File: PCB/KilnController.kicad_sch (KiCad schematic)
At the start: 19 parts, among them J1 12V 3A PS Header, J2 Exhaust Fan Header, J3 Circulation Fan Header, J4 SD Card Module, J5 Exhaust Servo Header, J6 Intake Servo Header, Q1 FQP30N06L, Q2 FQP30N06L, U1 Raspberry Pi Pico 2W

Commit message: Current monitoring WIP
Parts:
- J2, J3, J5, J6: footprint TerminalBlock_MetzConnect:TerminalBlock_MetzConnect_Type101_RT01604HBWC_1x04_P5.08mm_Horizontal -> KilnFootprintLibrary:TerminalBlock_MetzConnect_Type101_RT01604HBWC_1x04_P5.08mm_Horizontal; symbol Connector:Screw_Terminal_01x04 -> KilnSymbols:Screw_Terminal_01x04
- U1: footprint RasPi_Pico:RasPi_Pico_W_SMD -> Module:RaspberryPi_Pico_Common_THT
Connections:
- net SD_MISO: now also U1.6 (GP4); no longer U1.4 (GP2)
- net SD_SCK: now also U1.4 (GP2); no longer U1.6 (GP4)
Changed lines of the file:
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@@
 		)
 	)
-	(label "SD_MISO"
+	(label "SD_SCK"
 		(at 125.73 82.55 180)
 		(effects
@@
 		)
 	)
-	(label "SD_SCK"
+	(label "SD_MISO"
 		(at 125.73 87.63 180)
 		(effects
@@
 	)
 	(symbol
-		(lib_id "Connector:Screw_Terminal_01x04")
+		(lib_id "KilnSymbols:Screw_Terminal_01x04")
 		(at 246.38 134.62 90)
 		(unit 1)
@@
 			)
 		)
-		(property "Footprint" "TerminalBlock_MetzConnect:TerminalBlock_MetzConnect_Type101_RT01604HBWC_1x04_P5.08mm_Horizontal"
+		(property "Footprint" "KilnFootprintLibrary:TerminalBlock_MetzConnect_Type101_RT01604HBWC_1x04_P5.08mm_Horizontal"
 			(at 246.38 134.62 0)
 			(effects
@@
 			)
 		)
-		(property "Footprint" "RasPi_Pico:RasPi_Pico_W_SMD"
+		(property "Footprint" "Module:RaspberryPi_Pico_Common_THT"
 			(at 140.97 99.06 0)
 			(effects
@@
 	)
 	(symbol
-		(lib_id "Connector:Screw_Terminal_01x04")
+		(lib_id "KilnSymbols:Screw_Terminal_01x04")
 		(at 270.51 134.62 90)
 		(unit 1)
@@
 			)
 		)
-		(property "Footprint" "TerminalBlock_MetzConnect:TerminalBlock_MetzConnect_Type101_RT01604HBWC_1x04_P5.08mm_Horizontal"
+		(property "Footprint" "KilnFootprintLibrary:TerminalBlock_MetzConnect_Type101_RT01604HBWC_1x04_P5.08mm_Horizontal"
 			(at 270.51 134.62 0)
 			(effects
@@
 	)
 	(symbol
-		(lib_id "Connector:Screw_Terminal_01x04")
+		(lib_id "KilnSymbols:Screw_Terminal_01x04")
 		(at 245.11 78.74 90)
 		(unit 1)
@@
 			)
 		)
-		(property "Footprint" "TerminalBlock_MetzConnect:TerminalBlock_MetzConnect_Type101_RT01604HBWC_1x04_P5.08mm_Horizontal"
+		(property "Footprint" "KilnFootprintLibrary:TerminalBlock_MetzConnect_Type101_RT01604HBWC_1x04_P5.08mm_Horizontal"
 			(at 245.11 78.74 0)
 			(effects
@@
 	)
 	(symbol
-		(lib_id "Connector:Screw_Terminal_01x04")
+		(lib_id "KilnSymbols:Screw_Terminal_01x04")
 		(at 242.57 24.13 90)
 		(unit 1)
@@
 			)
 		)
-		(property "Footprint" "TerminalBlock_MetzConnect:TerminalBlock_MetzConnect_Type101_RT01604HBWC_1x04_P5.08mm_Horizontal"
+		(property "Footprint" "KilnFootprintLibrary:TerminalBlock_MetzConnect_Type101_RT01604HBWC_1x04_P5.08mm_Horizontal"
 			(at 242.57 24.13 0)
 			(effects

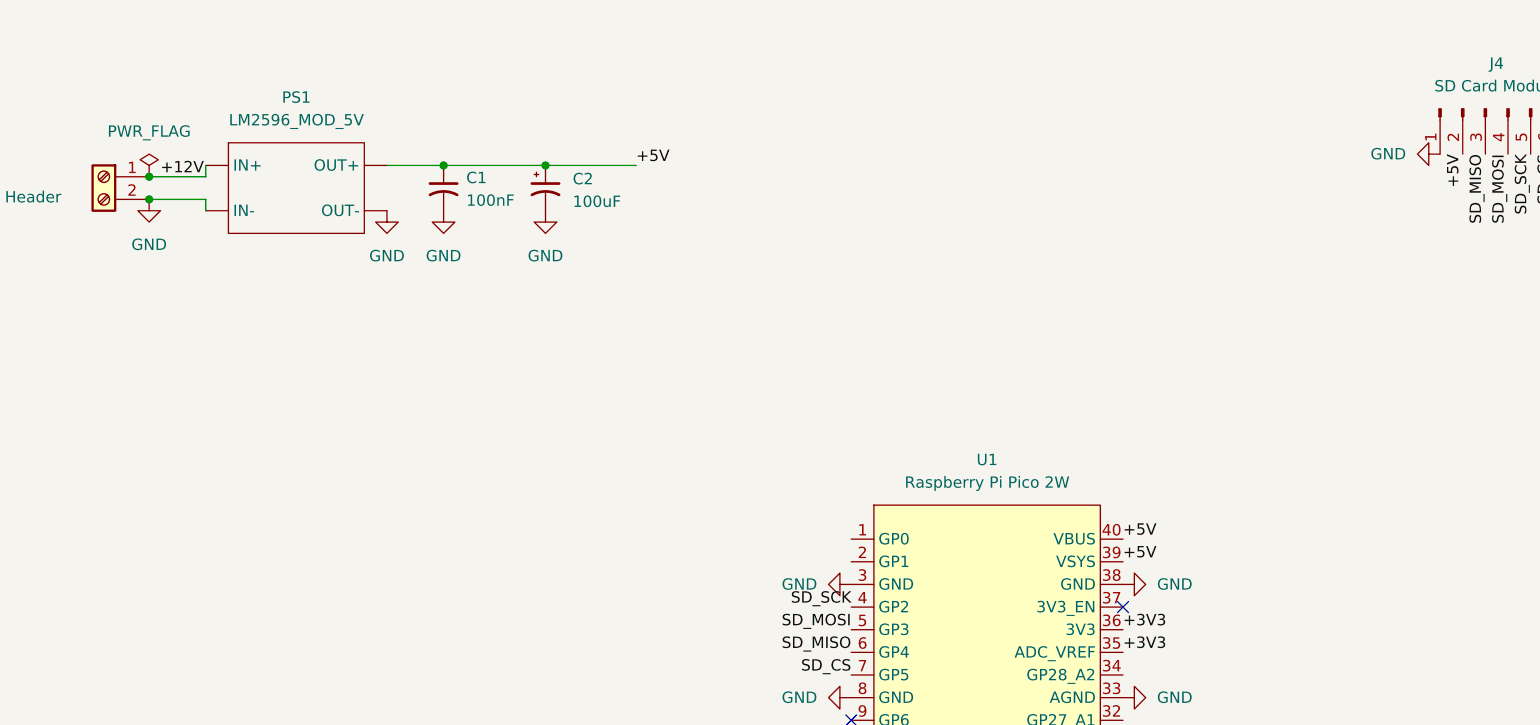
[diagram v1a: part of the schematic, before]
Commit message: Working current monitors, with updated layout
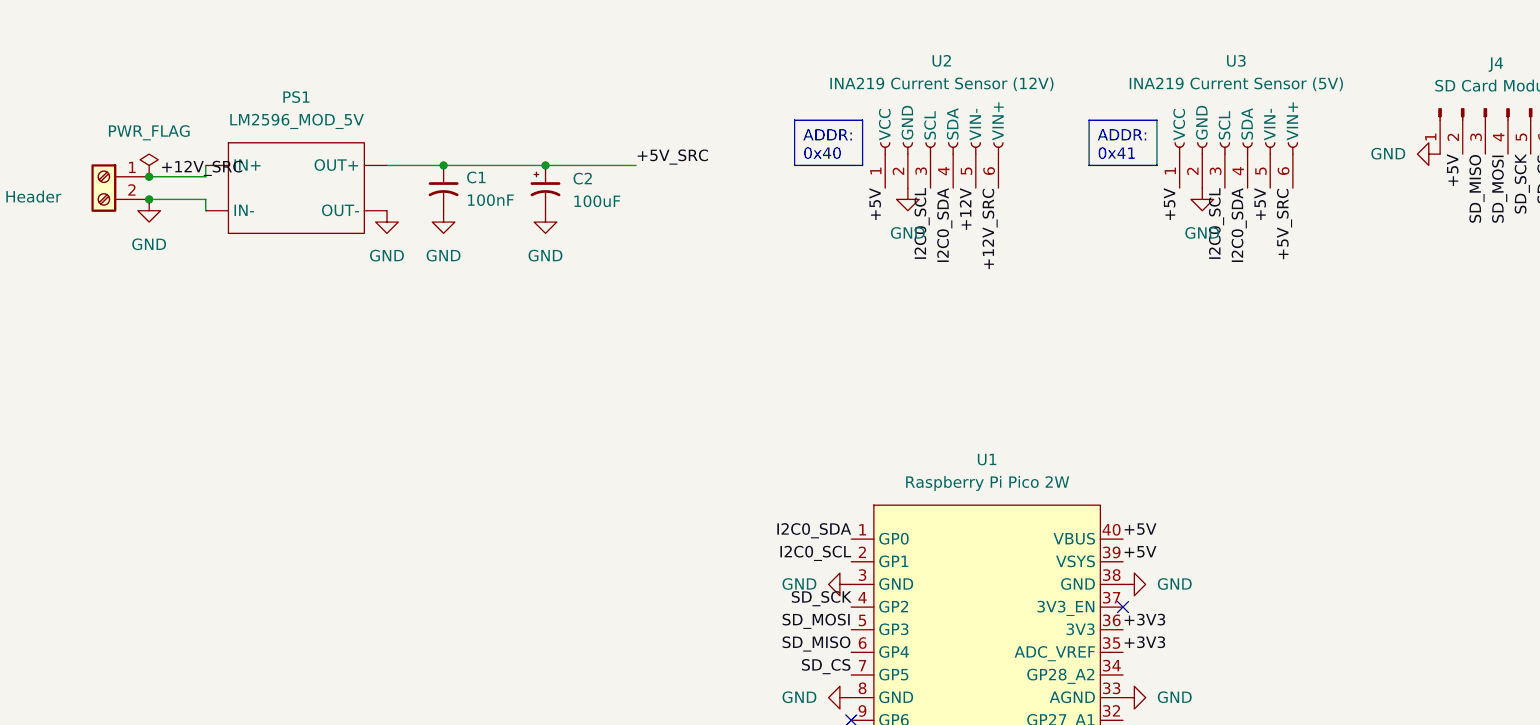
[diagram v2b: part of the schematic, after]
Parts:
- added U2: INA219 Current Sensor (12V), KilnFootprintLibrary:INA219_Module, symbol KilnSymbols:INA219_Current_Sensor_Module
- added U3: INA219 Current Sensor (5V), KilnFootprintLibrary:INA219_Module, symbol KilnSymbols:INA219_Current_Sensor_Module
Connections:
- net +12V: now also U2.5 (VIN-); no longer J1.1 (Pin_1), PS1.1 (IN+)
- net +5V: now also U2.1 (VCC), U3.1 (VCC), U3.5 (VIN-); no longer C1.1, C2.1, PS1.3 (OUT+)
- net GND: now also U2.2 (GND), U3.2 (GND)
- net I2C0_SDA: now reaches U1.1 (GP0)
- net I2C0_SDA: now also U2.4 (SDA), U3.4 (SDA)
- net I2C0_SCL: now reaches U1.2 (GP1)
- net I2C0_SCL: now also U2.3 (SCL), U3.3 (SCL)
- new net +12V_SRC: J1.1 (Pin_1), PS1.1 (IN+), U2.6 (VIN+)
- new net +5V_SRC: C1.1, C2.1, PS1.3 (OUT+), U3.6 (VIN+)

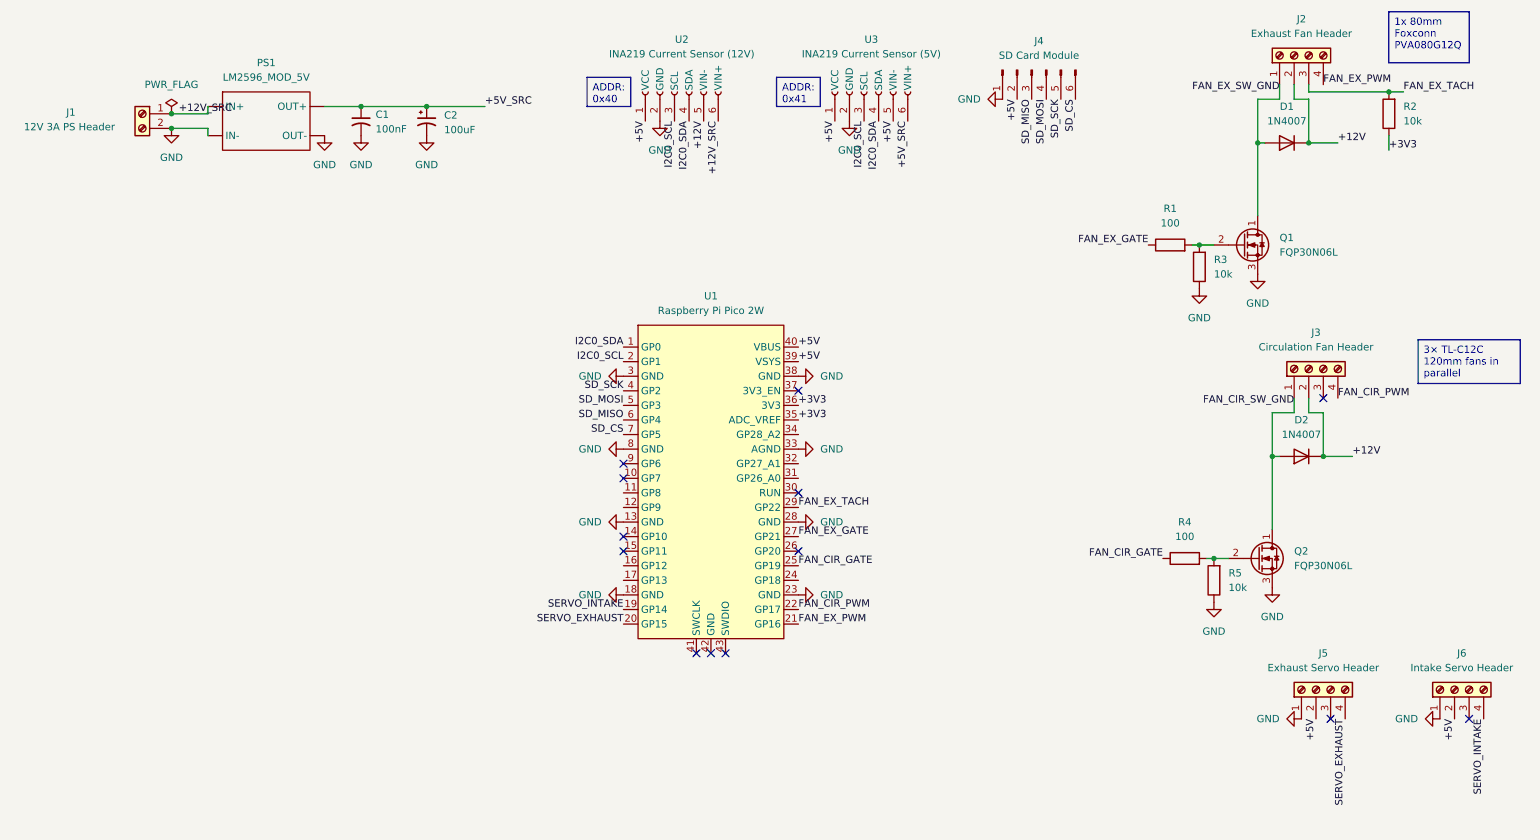
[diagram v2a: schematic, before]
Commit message: Controller and KiCad for SHT31D sensors
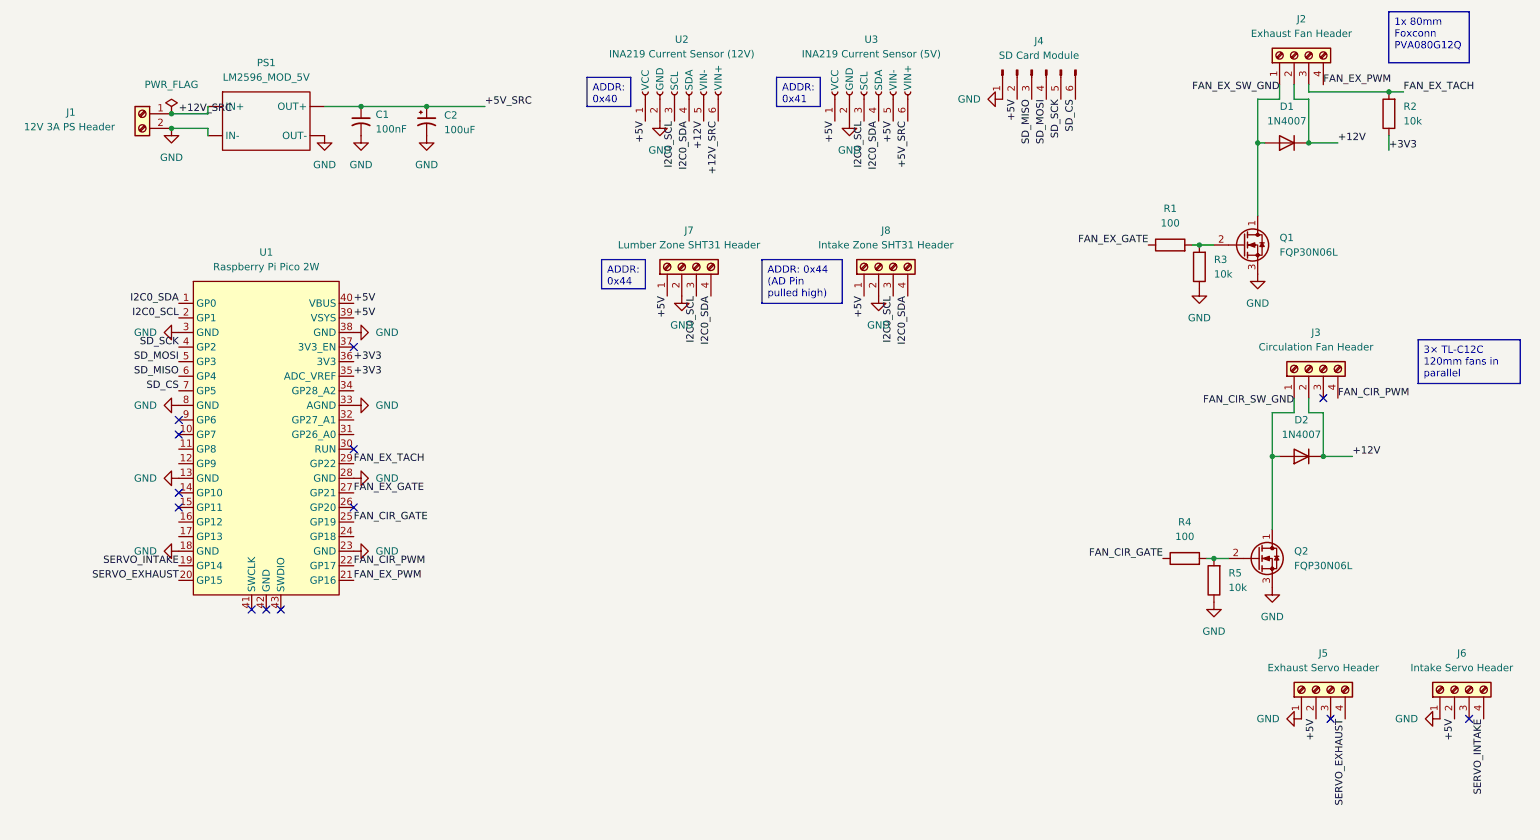
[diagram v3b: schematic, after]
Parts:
- added J7: Lumber Zone SHT31 Header, KilnFootprintLibrary:TerminalBlock_MetzConnect_Type101_RT01604HBWC_1x04_P5.08mm_Horizontal, symbol KilnSymbols:Screw_Terminal_01x04
- added J8: Intake Zone SHT31 Header, KilnFootprintLibrary:TerminalBlock_MetzConnect_Type101_RT01604HBWC_1x04_P5.08mm_Horizontal, symbol KilnSymbols:Screw_Terminal_01x04
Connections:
- net +5V: now also J7.1 (Pin_1), J8.1 (Pin_1)
- net GND: now also J7.2 (Pin_2), J8.2 (Pin_2)
- net I2C0_SCL: now also J7.3 (Pin_3), J8.3 (Pin_3)
- net I2C0_SDA: now also J7.4 (Pin_4), J8.4 (Pin_4)
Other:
- moved on the sheet: U1

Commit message: Heater SSR controller and PCB update
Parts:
- added J9: Heater SSR Header, TerminalBlock_MetzConnect:TerminalBlock_MetzConnect_Type101_RT01602HBWC_1x02_P5.08mm_Horizontal, symbol Connector:Screw_Terminal_01x02
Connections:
- net GND: now also J9.2 (Pin_2)
- net HEATER_SSR: now reaches U1.24 (GP18)
- net HEATER_SSR: now also J9.1 (Pin_1)
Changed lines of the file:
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@@
+		)
+	)
+	(label "HEATER_SSR"
+		(at 78.74 107.95 0)
+		(effects
+			(font
+				(size 1.27 1.27)
+			)
+			(justify left bottom)
 		)
 	)
@@
 	(label "I2C0_SDA"
 		(at 140.97 66.04 270)
+		(effects
+			(font
+				(size 1.27 1.27)
+			)
+			(justify right bottom)
+		)
+	)
+	(label "HEATER_SSR"
+		(at 173.99 92.71 270)
 		(effects
 			(font
@@
 	)
 	(symbol
+		(lib_id "Connector:Screw_Terminal_01x02")
+		(at 173.99 87.63 90)
+		(unit 1)
+		(exclude_from_sim no)
+		(in_bom yes)
+		(on_board yes)
+		(dnp no)
+		(property "Reference" "J9"
+			(at 175.006 80.518 90)
+			(effects
+				(font
+					(size 1.27 1.27)
+				)
+			)
+		)
+		(property "Value" "Heater SSR Header"
+			(at 175.26 83.058 90)
+			(effects
+				(font
+					(size 1.27 1.27)
+				)
+			)
+		)
+		(property "Footprint" "TerminalBlock_MetzConnect:TerminalBlock_MetzConnect_Type101_RT01602HBWC_1x02_P5.08mm_Horizontal"
+			(at 173.99 87.63 0)
+			(effects
+				(font
+					(size 1.27 1.27)
+				)
+				(hide yes)
+			)
+		)
+		(property "Datasheet" "~"
+			(at 173.99 87.63 0)
+			(effects
+				(font
+					(size 1.27 1.27)
+				)
+				(hide yes)
+			)
+		)
+		(property "Description" "Generic screw terminal, single row, 01x02, script generated (kicad-library-utils/schlib/autogen/connector/)"
+			(at 173.99 87.63 0)
+			(effects
+				(font
+					(size 1.27 1.27)
+				)
+				(hide yes)
+			)
+		)
+		(pin "2"
+		)
+		(pin "1"
+		)
+		(instances
+			(project "KilnController"
+				(path "/c3036073-6461-4b90-ba15-ffed45812946"
+					(reference "J9")
+					(unit 1)
+				)
+			)
+		)
+	)
+	(symbol
 		(lib_id "Device:R")
 		(at 259.08 34.29 180)
@@
 					(unit 1)
 				)
+			)
+		)
+	)
+	(symbol
+		(lib_id "power:GND")
+		(at 176.53 92.71 0)
+		(unit 1)
+		(exclude_from_sim no)
+		(in_bom yes)
+		(on_board yes)
+		(dnp no)
+		(fields_autoplaced yes)
+		(property "Reference" "#PWR024"
+			(at 176.53 99.06 0)
+			(effects
+				(font
+					(size 1.27 1.27)
+				)
+				(hide yes)
+			)
+		)
+		(property "Value" "GND"
+			(at 176.53 97.79 0)
+			(effects
+				(font
+					(size 1.27 1.27)
+				)
+			)
+		)
+		(property "Footprint" ""
+			(at 176.53 92.71 0)
+			(effects
+				(font
+					(size 1.27 1.27)
+				)
+				(hide yes)
+			)
+		)
+		(property "Datasheet" ""
+			(at 176.53 92.71 0)
+			(effects
+				(font
+					(size 1.27 1.27)
+				)
+				(hide yes)
+			)
+		)
+		(property "Description" "Power symbol creates a global label with name \"GND\" , ground"
+			(at 176.53 92.71 0)
+			(effects
+				(font
+					(size 1.27 1.27)
+				)
+				(hide yes)
+			)
+		)
+		(pin "1"
+		)
+		(instances
+			(project "KilnController"
+				(path "/c3036073-6461-4b90-ba15-ffed45812946"
+					(reference "#PWR024")
+					(unit 1)
+				)

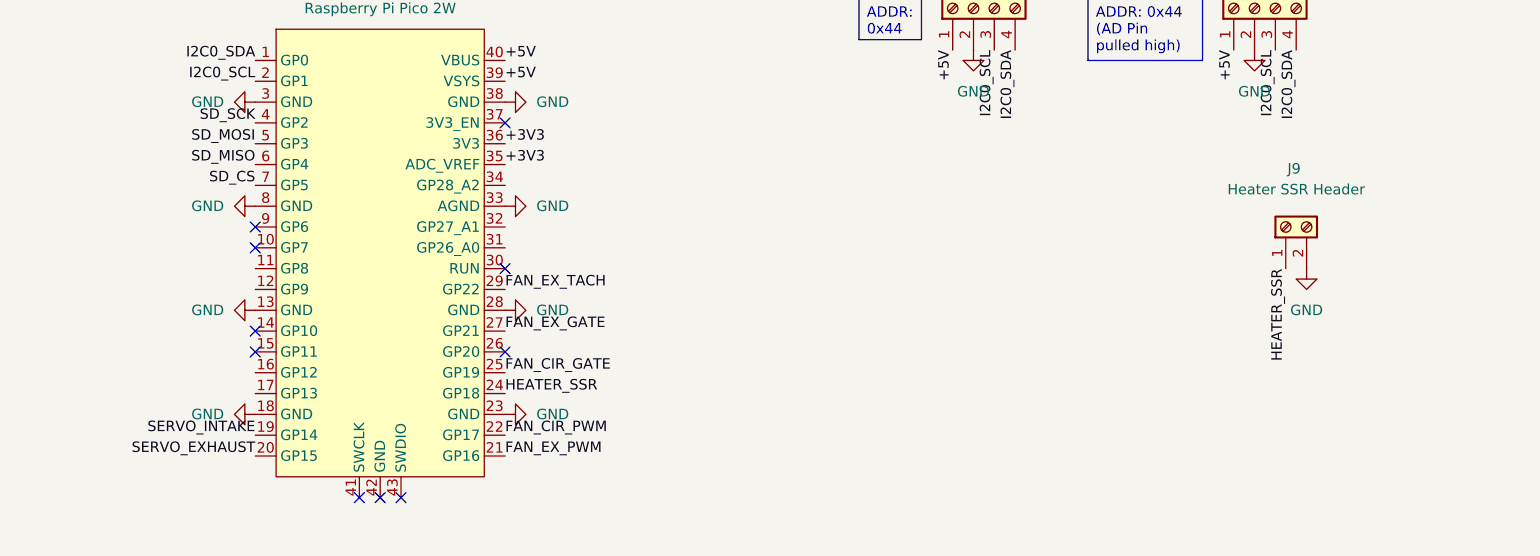
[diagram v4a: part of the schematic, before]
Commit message: Working display driver with schematic and layout
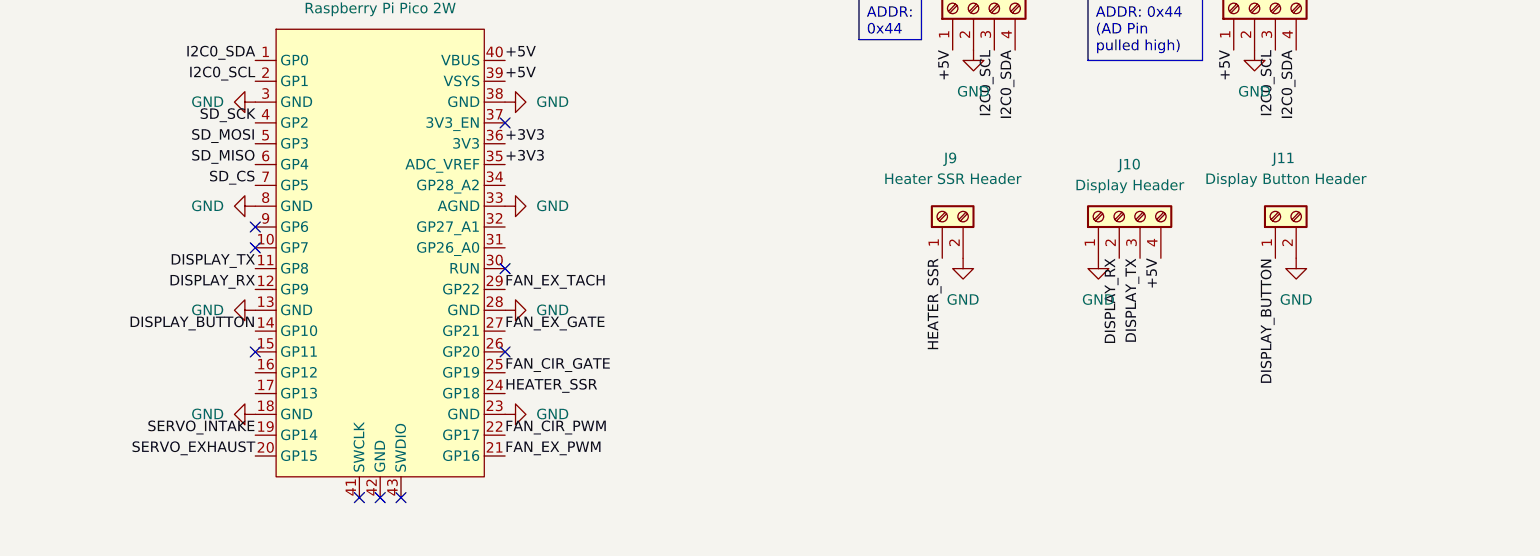
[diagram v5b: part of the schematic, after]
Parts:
- added J10: Display Header, KilnFootprintLibrary:TerminalBlock_MetzConnect_Type101_RT01604HBWC_1x04_P5.08mm_Horizontal, symbol KilnSymbols:Screw_Terminal_01x04
- added J11: Display Button Header, TerminalBlock_MetzConnect:TerminalBlock_MetzConnect_Type101_RT01602HBWC_1x02_P5.08mm_Horizontal, symbol Connector:Screw_Terminal_01x02
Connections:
- net +5V: now also J10.4 (Pin_4)
- net GND: now also J10.1 (Pin_1), J11.2 (Pin_2)
- net DISPLAY_TX: now reaches U1.11 (GP8)
- net DISPLAY_TX: now also J10.3 (Pin_3)
- net DISPLAY_RX: now reaches U1.12 (GP9)
- net DISPLAY_RX: now also J10.2 (Pin_2)
- net DISPLAY_BUTTON: now reaches U1.14 (GP10)
- net DISPLAY_BUTTON: now also J11.1 (Pin_1)
- no-connect marks 13 -> 12
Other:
- moved on the sheet: J9
